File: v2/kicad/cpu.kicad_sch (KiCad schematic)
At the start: 3 parts, among them U3 W65C02SxP

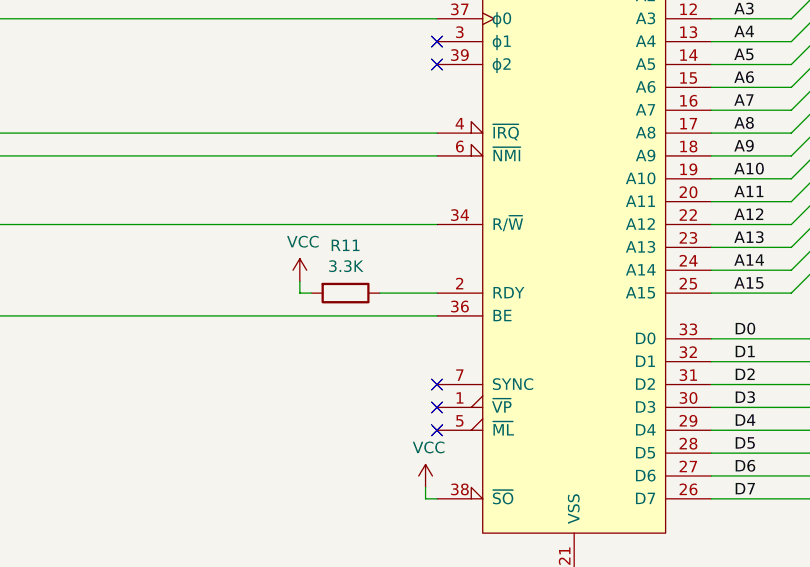
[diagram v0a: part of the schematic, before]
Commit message: PCB Tweaks
Tracks optimized.
SMD components moved to top layer.
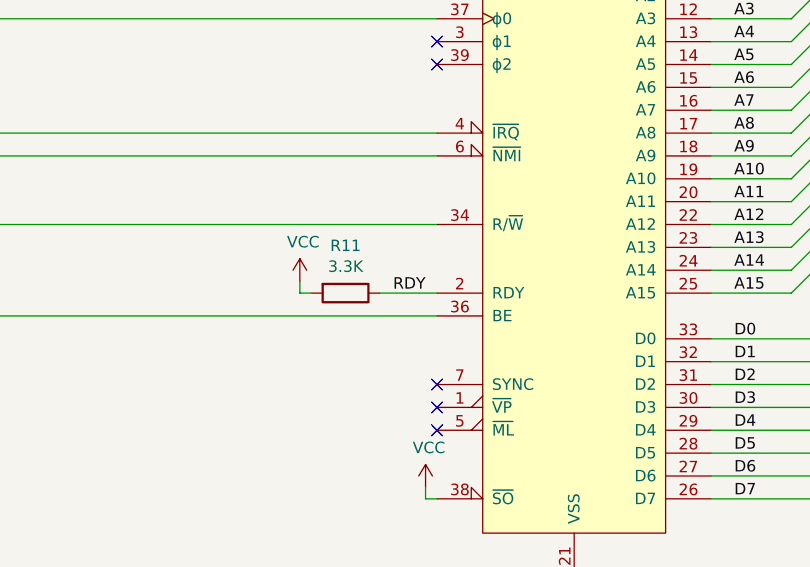
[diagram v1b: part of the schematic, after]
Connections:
- net RDY: now reaches R11.1, U3.2 (RDY)
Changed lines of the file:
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@@
   (paper "A4")
   (junction (at 71.12 93.98) (diameter 1.016) (color 0 0 0 0))
+  (no_connect (at 142.24 121.92))
+  (no_connect (at 142.24 83.82))
+  (no_connect (at 142.24 86.36))
+  (no_connect (at 142.24 127))
   (no_connect (at 142.24 124.46))
-  (no_connect (at 142.24 86.36))
-  (no_connect (at 142.24 83.82))
-  (no_connect (at 142.24 121.92))
-  (no_connect (at 142.24 127))
   (bus_entry (at 181.61 73.66) (size 2.54 -2.54)
     (stroke (width 0.1524) (type solid) (color 0 0 0 0))
@@
     (stroke (width 0) (type solid) (color 0 0 0 0))
   )
+  (label "RDY" (at 140.97 111.76 180)
+    (effects (font (size 1.27 1.27)) (justify right bottom))
+  )
   (label "D[0..7]" (at 170.18 39.37 0)
